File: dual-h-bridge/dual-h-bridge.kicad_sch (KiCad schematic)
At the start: 42 parts, among them J1 Motor0, J2 Motor1, J3 BATT, J4 MCU, Q1 2N3904, Q2 2N3904, U1 LT1161

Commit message: Change name and produce production outputs
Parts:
- S1: footprint GS_Virtual:ENPH253_Logo_Small -> GS_Virtual:ENPH253_Logo; now left out of the parts list
- TP10, TP11, TP12, TP17, TP18, TP19, TP5, TP6, TP7, TP8, TP9: now left out of the parts list
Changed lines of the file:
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@@
 		(unit 1)
 		(exclude_from_sim no)
-		(in_bom yes)
+		(in_bom no)
 		(on_board yes)
 		(dnp no)
@@
 		(unit 1)
 		(exclude_from_sim no)
-		(in_bom yes)
+		(in_bom no)
 		(on_board yes)
 		(dnp no)
@@
 		(unit 1)
 		(exclude_from_sim no)
-		(in_bom yes)
+		(in_bom no)
 		(on_board yes)
 		(dnp no)
@@
 		(unit 1)
 		(exclude_from_sim no)
-		(in_bom yes)
+		(in_bom no)
 		(on_board yes)
 		(dnp no)
@@
 		(unit 1)
 		(exclude_from_sim no)
-		(in_bom yes)
+		(in_bom no)
 		(on_board yes)
 		(dnp no)
@@
 		(unit 1)
 		(exclude_from_sim no)
-		(in_bom yes)
+		(in_bom no)
 		(on_board yes)
 		(dnp no)
@@
 		(unit 1)
 		(exclude_from_sim no)
-		(in_bom yes)
+		(in_bom no)
 		(on_board yes)
 		(dnp no)
@@
 		(unit 1)
 		(exclude_from_sim no)
-		(in_bom yes)
+		(in_bom no)
 		(on_board yes)
 		(dnp no)
@@
 		(unit 1)
 		(exclude_from_sim no)
-		(in_bom yes)
+		(in_bom no)
 		(on_board yes)
 		(dnp no)
@@
 		(unit 1)
 		(exclude_from_sim no)
-		(in_bom yes)
+		(in_bom no)
 		(on_board yes)
 		(dnp no)
@@
 		(unit 1)
 		(exclude_from_sim no)
-		(in_bom yes)
+		(in_bom no)
 		(on_board yes)
 		(dnp no)
@@
 			)
 		)
-		(property "Footprint" "GS_Virtual:ENPH253_Logo_Small"
+		(property "Footprint" "GS_Virtual:ENPH253_Logo"
 			(at 290.83 279.4 0)
 			(effects
@@
 		(unit 1)
 		(exclude_from_sim no)
-		(in_bom yes)
+		(in_bom no)
 		(on_board yes)
 		(dnp no)

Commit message: Update to right angle motor connectors
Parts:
- J1, J2: footprint Connector_JST:JST_XH_B2B-XH-A_1x02_P2.50mm_Vertical -> GS_Connectors:JST_XH_S2B-XH-A-1_1x02_P2.50mm_Horizontal
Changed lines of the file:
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@@
 			)
 		)
-		(property "Footprint" "Connector_JST:JST_XH_B2B-XH-A_1x02_P2.50mm_Vertical"
+		(property "Footprint" "GS_Connectors:JST_XH_S2B-XH-A-1_1x02_P2.50mm_Horizontal"
 			(at 387.35 114.3 0)
 			(effects
@@
 			)
 		)
-		(property "Footprint" "Connector_JST:JST_XH_B2B-XH-A_1x02_P2.50mm_Vertical"
+		(property "Footprint" "GS_Connectors:JST_XH_S2B-XH-A-1_1x02_P2.50mm_Horizontal"
 			(at 387.35 168.91 0)
 			(effects
@@
 		)
 		(instances
-			(project "motor-controller"
+			(project "dual-h-bridge"
 				(path "/3cf627b4-179f-4b19-ad57-a5207e12b14c"
 					(page "3")
@@
 		)
 		(instances
-			(project "motor-controller"
+			(project "dual-h-bridge"
 				(path "/3cf627b4-179f-4b19-ad57-a5207e12b14c"
 					(page "2")
@@
 		)
 		(instances
-			(project "motor-controller"
+			(project "dual-h-bridge"
 				(path "/3cf627b4-179f-4b19-ad57-a5207e12b14c"
 					(page "5")
@@
 		)
 		(instances
-			(project "motor-controller"
+			(project "dual-h-bridge"
 				(path "/3cf627b4-179f-4b19-ad57-a5207e12b14c"
 					(page "4")

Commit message: Fix potentially inverted H-Bridge direction bit
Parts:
- S1: footprint GS_Virtual:ENPH253_Logo -> GS_Virtual:ENPH253_Logo_Small
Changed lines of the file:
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@@
 	(title_block
 		(title "Motor Controller")
-		(date "2025-06-14")
-		(rev "A")
+		(date "2025-07-05")
+		(rev "v2.0.0")
 		(company "Team 5")
 		(comment 1 "George Sleen")
@@
 			)
 		)
-		(property "Footprint" "GS_Virtual:ENPH253_Logo"
+		(property "Footprint" "GS_Virtual:ENPH253_Logo_Small"
 			(at 290.83 279.4 0)
 			(effects

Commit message: Update silkscreen
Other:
- title: Motor Controller -> Dual H-Bridge
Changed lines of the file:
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@@
 	(paper "A3")
 	(title_block
-		(title "Motor Controller")
-		(date "2025-07-05")
-		(rev "v2.0.0")
+		(title "Dual H-Bridge")
+		(date "2025-07-06")
+		(rev "v2.0.1")
 		(company "Team 5")
 		(comment 1 "George Sleen")

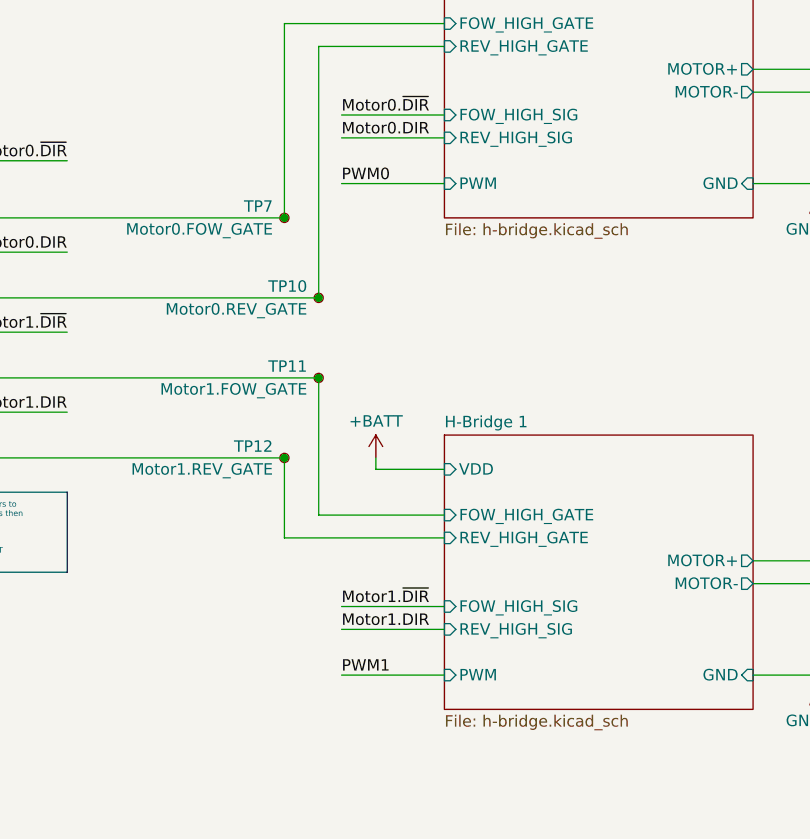
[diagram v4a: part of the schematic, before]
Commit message: Fix optocoupler hardware issue
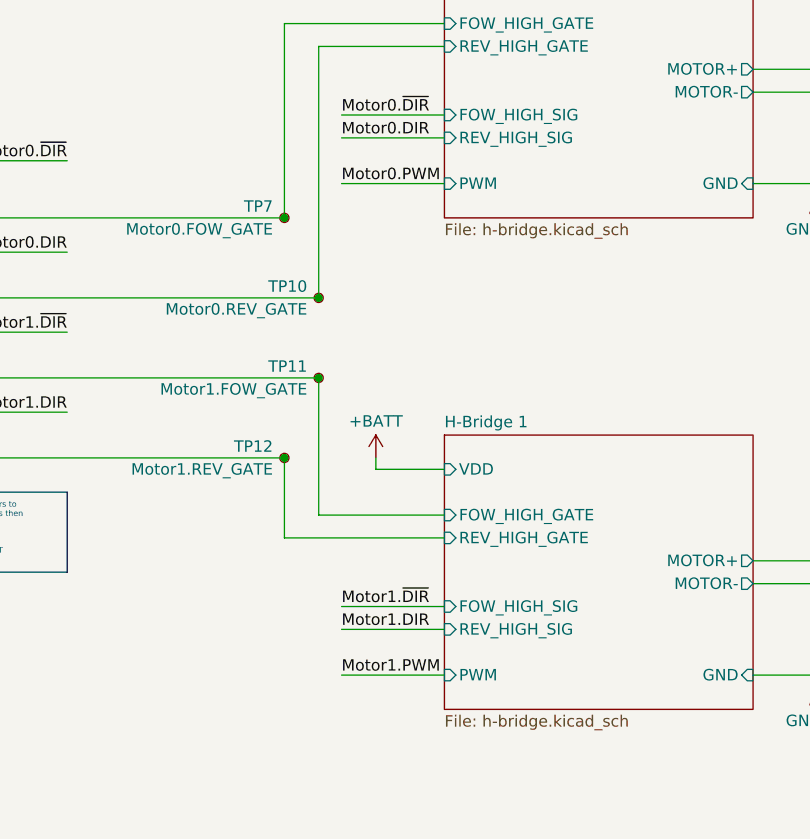
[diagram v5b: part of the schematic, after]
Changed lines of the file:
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@@
 	(title_block
 		(title "Dual H-Bridge")
-		(date "2025-07-06")
-		(rev "v2.0.1")
+		(date "2025-07-09")
+		(rev "v3.0.0")
 		(company "Team 5")
 		(comment 1 "George Sleen")
@@
 		)
 	)
-	(label "PWM1"
-		(at 318.77 181.61 0)
-		(effects
-			(font
-				(size 1.27 1.27)
-			)
-			(justify left bottom)
-		)
-	)
 	(label "Motor1.~{DIR}"
 		(at 218.44 133.35 180)
@@
 		)
 	)
+	(label "Motor1.PWM"
+		(at 318.77 181.61 0)
+		(effects
+			(font
+				(size 1.27 1.27)
+			)
+			(justify left bottom)
+		)
+	)
 	(label "MCU.DIR0"
 		(at 39.37 158.75 0)
@@
 		)
 	)
+	(label "Motor0.PWM"
+		(at 318.77 127 0)
+		(effects
+			(font
+				(size 1.27 1.27)
+			)
+			(justify left bottom)
+		)
+	)
 	(label "Motor1.~{DIR}"
 		(at 318.77 173.99 0)
@@
 		(effects
 			(font
-				(size 1.27 1.27)
-			)
-			(justify left bottom)
-		)
-	)
-	(label "PWM0"
-		(at 318.77 127 0)
-		(effects
-			(font

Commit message: Some small updates
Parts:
- R1, R3: value 10k -> 1k
- R2, R4: value 100k -> 10k
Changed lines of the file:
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@@
 		(title "Dual H-Bridge")
 		(date "2025-07-09")
-		(rev "v3.0.0")
+		(rev "v4.0.0")
 		(company "Team 5")
 		(comment 1 "George Sleen")
@@
 			)
 		)
-		(property "Value" "10k"
+		(property "Value" "1k"
 			(at 137.16 167.6399 0)
 			(effects
@@
 			)
 		)
-		(property "Value" "100k"
+		(property "Value" "10k"
 			(at 123.19 172.72 90)
 			(effects
@@
 			)
 		)
-		(property "Value" "10k"
+		(property "Value" "1k"
 			(at 137.16 109.2199 0)
 			(effects
@@
 			)
 		)
-		(property "Value" "100k"
+		(property "Value" "10k"
 			(at 123.19 114.3 90)
 			(effects

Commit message: More changes
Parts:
- R1, R3: value 1k -> 10k
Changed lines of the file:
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@@
 			)
 		)
-		(property "Value" "1k"
+		(property "Value" "10k"
 			(at 137.16 167.6399 0)
 			(effects
@@
 			)
 		)
-		(property "Value" "1k"
+		(property "Value" "10k"
 			(at 137.16 109.2199 0)
 			(effects

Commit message: Fix all hardware issues and generate final release source files
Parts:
- added TP12: Motor0.PWM, TestPoint:TestPoint_Pad_1.5x1.5mm, symbol Connector:TestPoint_Small
- added TP13: Motor1.PWM, TestPoint:TestPoint_Pad_1.5x1.5mm, symbol Connector:TestPoint_Small
- C1, C2, C3, C4, C5, C6, C8: symbol GS_Capacitor_THT:C_THT_100nF -> GS_Capacitor_THT:C_THT_Ceramic_Disk
- C10: renamed from C9; symbol GS_Capacitor_THT:C_THT_100nF -> GS_Capacitor_THT:C_THT_Ceramic_Disk
- C11: renamed from C10; symbol GS_Capacitor_THT:C_THT_100nF -> GS_Capacitor_THT:C_THT_Ceramic_Disk
- C12: renamed from C11; symbol GS_Capacitor_THT:C_THT_100nF -> GS_Capacitor_THT:C_THT_Ceramic_Disk
- C9: renamed from C12; symbol GS_Capacitor_THT:C_THT_100nF -> GS_Capacitor_THT:C_THT_Ceramic_Disk
- renumbered J4 to J2, J2 to J3, J3 to J4, TP5 to TP1, TP18 to TP10, TP19 to TP11, TP6 to TP2, TP7 to TP3, TP8 to TP4, TP9 to TP5, TP10 to TP6, TP11 to TP7, TP12 to TP8, TP17 to TP9
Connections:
- net Motor0.PWM: now also TP12.1
- net Motor1.PWM: now also TP13.1
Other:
- moved on the sheet: J1, J3, TP3, TP6, TP7, TP8
